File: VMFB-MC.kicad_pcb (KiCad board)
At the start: 2 copper layers, 64.6 x 73.2 mm, 50 parts, among them J1 DISPENSE, J2 EMPTY, J3 DISPENSE, J4 EMPTY, J5 DEPOSIT, J6 DISPENSE, J7 MOTOR, J8 PIR, J9 Conn_01x10_Pin, Q1 Q_Photo_NPN, Q10 Q_Photo_NPN, Q2 Q_Photo_NPN, Q3 Q_Photo_NPN, Q4 Q_Photo_NPN, Q5 Q_Photo_NPN, Q6 Q_Photo_NPN, Q7 TIP120, Q8 TIP120, Q9 BC337, U1 LM393

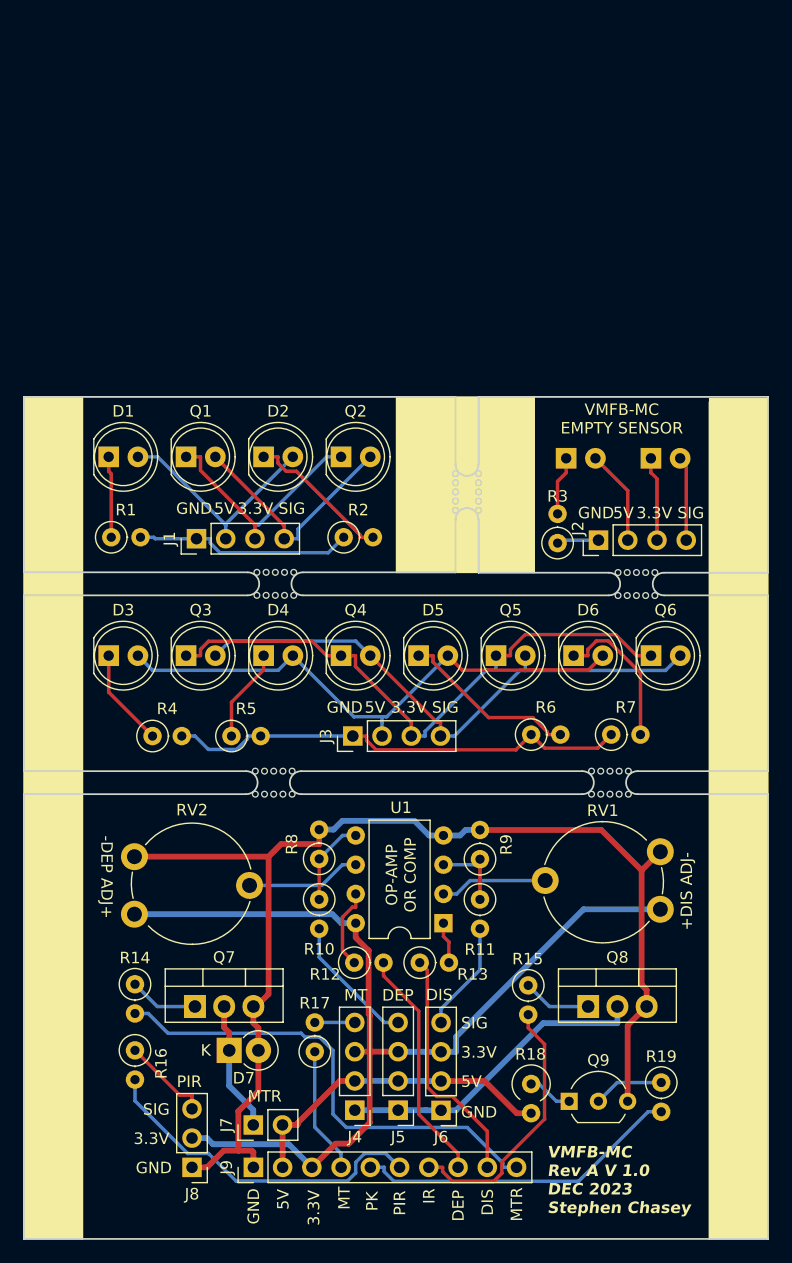
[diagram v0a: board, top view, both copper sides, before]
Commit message: reduced footprint
footprint is now 65x68mm
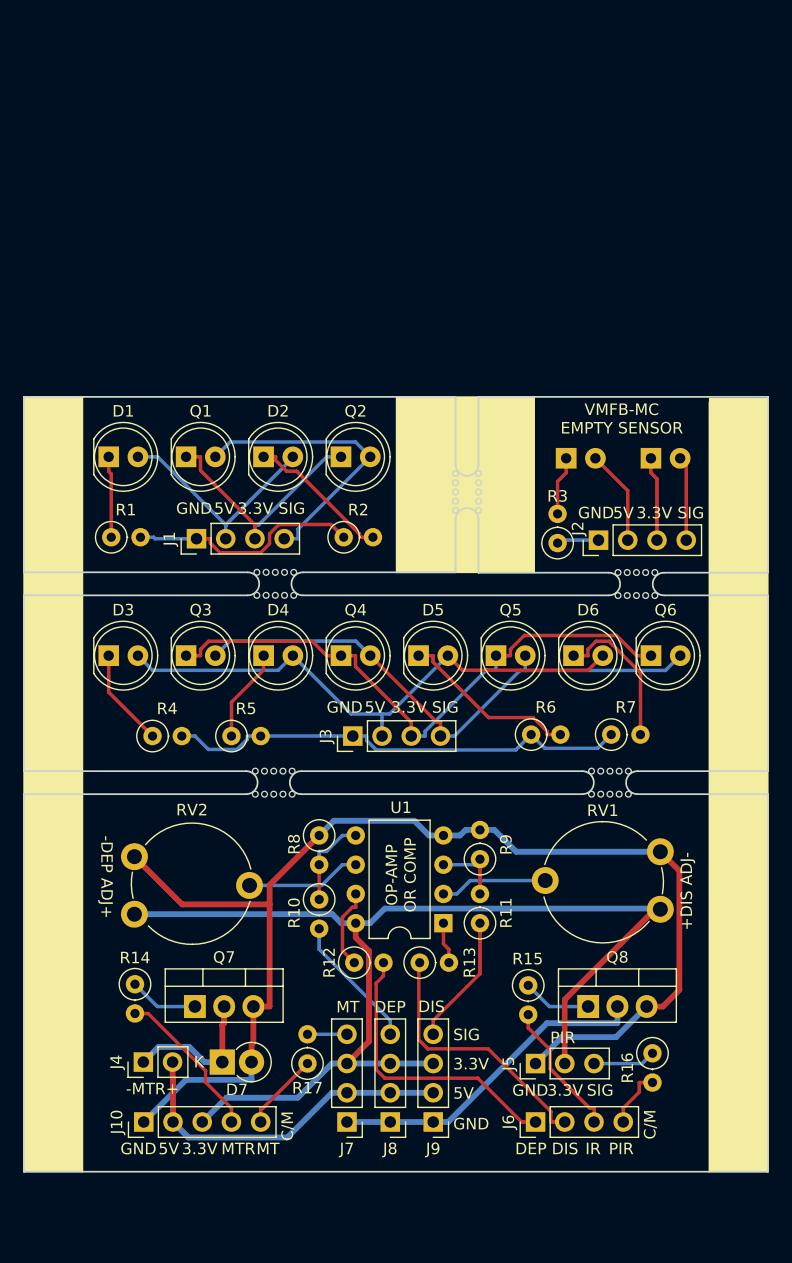
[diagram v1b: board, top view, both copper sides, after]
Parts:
- removed the G*** at (132.6, 103.9)
- removed the J9 at (120.0, 117.0)
- removed the Q9 at (147.4, 111.2)
- removed R18: 47R, Resistor_THT:R_Axial_DIN0309_L9.0mm_D3.2mm_P2.54mm_Vertical
- removed R19: 10K, Resistor_THT:R_Axial_DIN0207_L6.3mm_D2.5mm_P2.54mm_Vertical
- added G***: LOGO, VMFB-MC:VMFB_logo_20mm, B.Cu at (132.7, 97.7)
- added J10: Conn_01x05_Pin, Connector_PinHeader_2.54mm:PinHeader_1x05_P2.54mm_Vertical, F.Cu at (110.5, 113.0)
- added J6: Conn_01x04_Pin, Connector_PinHeader_2.54mm:PinHeader_1x04_P2.54mm_Vertical, F.Cu at (144.5, 113.0)
- moved R16 45.0 mm to (154.7, 107.1)
- moved J5 31.2 mm to (144.5, 108.0), turned to 90 degrees
- moved J4 11.0 mm to (110.5, 107.8)
- moved R11 2.06 mm to (139.7, 95.8), turned to 90 degrees
- moved R8 2.03 mm to (125.7, 88.1), turned to -90 degrees
- moved J7 1.23 mm to (128.1, 113.0)
- moved J8 1.23 mm to (131.9, 113.0)
- moved J9 1.22 mm to (135.6, 113.0)
- moved R17 1.21 mm to (124.7, 108.0)
- moved D7 1.18 mm to (117.3, 107.8)
- renumbered J7 to J4, J8 to J5, J4 to J7, J5 to J8, J6 to J9, Q10 to Q9
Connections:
- R11 pad 1: Net-(U1A-+) -> DISPENSE SIG
- R11 pad 2: DISPENSE SIG -> Net-(U1A-+)
- R8 pad 1: Net-(U1B-+) -> GND
- R8 pad 2: GND -> Net-(U1B-+)
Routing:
- net MOTOR: track 42.1 -> 13.6 mm
- net PBKA: track 28.5 -> 0.00 mm
- net PIR: track 29.8 -> 5.16 mm
- net SENSOR IR: track 23.3 -> 11.9 mm
- net +3.3V: track 87.9 -> 99.3 mm
- net Net-(Q9-B): track 6.14 -> 0.00 mm
- net Net-(J1-Pin_4): track 20.5 -> 25.4 mm
- net DEPOSIT: track 20.5 -> 25.3 mm
- net EMPTY: track 11.0 -> 6.87 mm
- net Net-(Q9-C): track 3.92 -> 0.00 mm
- net GND: track 106.0 -> 108.4 mm
- net Net-(J5-Pin_3): track 7.76 -> 5.45 mm
- net DISPENSE: track 21.0 -> 22.9 mm
- net +5V: track 28.1 -> 30.0 mm
- net DISPENSE SIG: track 9.56 -> 11.3 mm
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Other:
- board size 64.6 x 73.2 mm -> 64.6 x 67.3 mm
- board text added: "-MTR+"
- board text added: "C/M"
- board text removed: "PK"

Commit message: MT bleeder resistor
Added bleeder resistor to the MT sensor.
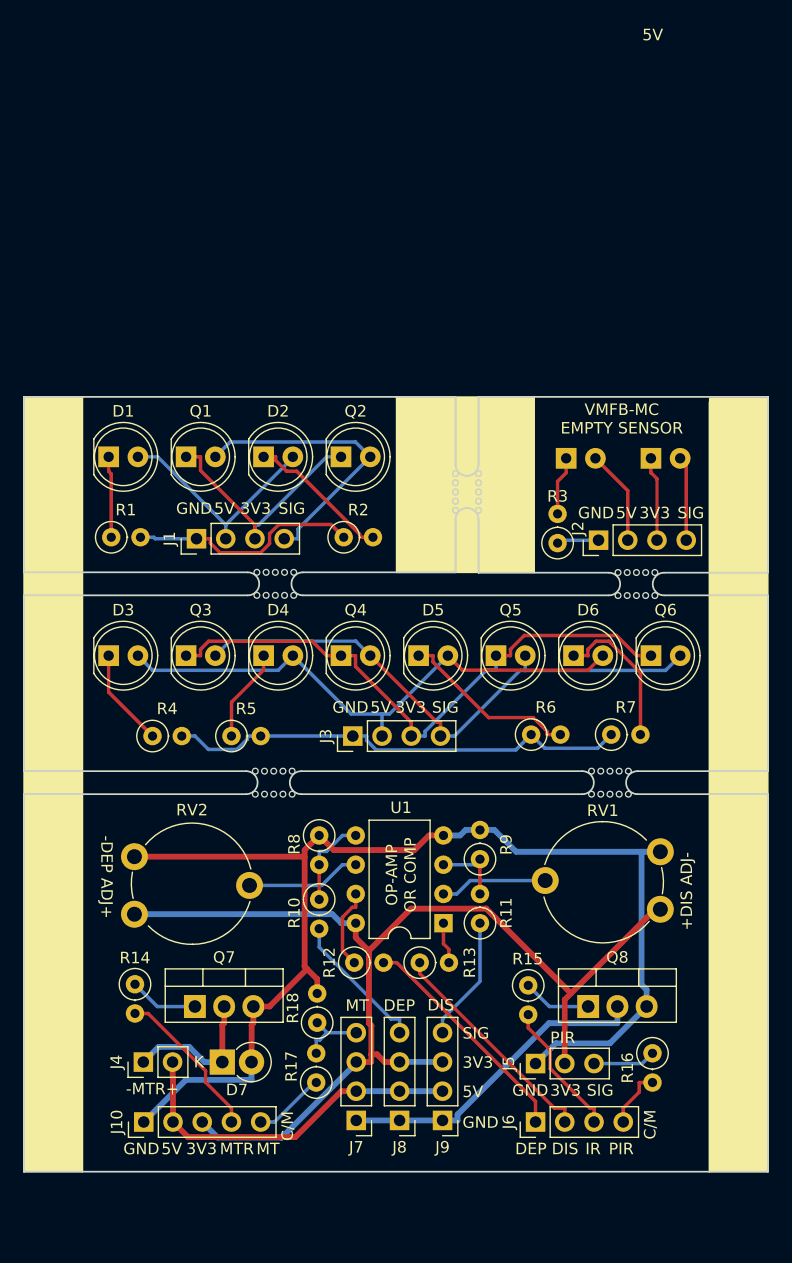
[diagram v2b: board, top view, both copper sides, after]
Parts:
- added R18: 10K, Resistor_THT:R_Axial_DIN0207_L6.3mm_D2.5mm_P2.54mm_Vertical, F.Cu at (125.6, 104.4)
- moved R17 1.82 mm to (125.5, 109.6)
- moved J7 0.82 mm to (129.0, 112.9)
- moved J8 0.82 mm to (132.7, 112.9)
- moved J9 0.82 mm to (136.4, 112.9)
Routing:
- net DEPOSIT: track 25.3 -> 20.0 mm
- net +3.3V: track 99.3 -> 95.9 mm
- net DISPENSE: track 22.9 -> 19.6 mm
- net Net-(J7-Pin_4): track 3.43 -> 6.12 mm
- net GND: track 108.4 -> 109.8 mm
- net +5V: track 30.0 -> 30.8 mm
- net DEPOSIT SIG: track 11.7 -> 12.4 mm
- net EMPTY: track 6.87 -> 6.25 mm
- net IR GND: track 28.5 -> 27.9 mm
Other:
- board text added: "3V3"
- board text removed: "3.3V"

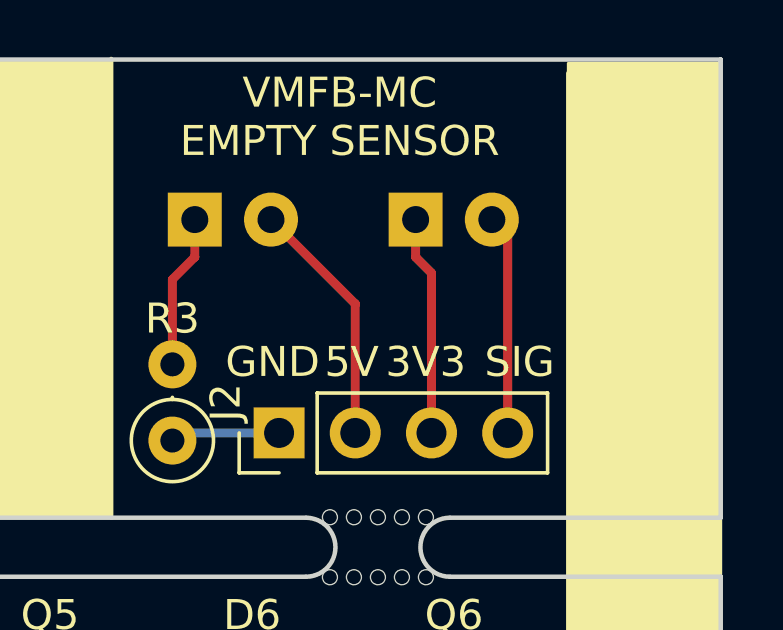
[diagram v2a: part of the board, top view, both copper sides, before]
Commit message: Cleaned up tracks placement on MT sensor
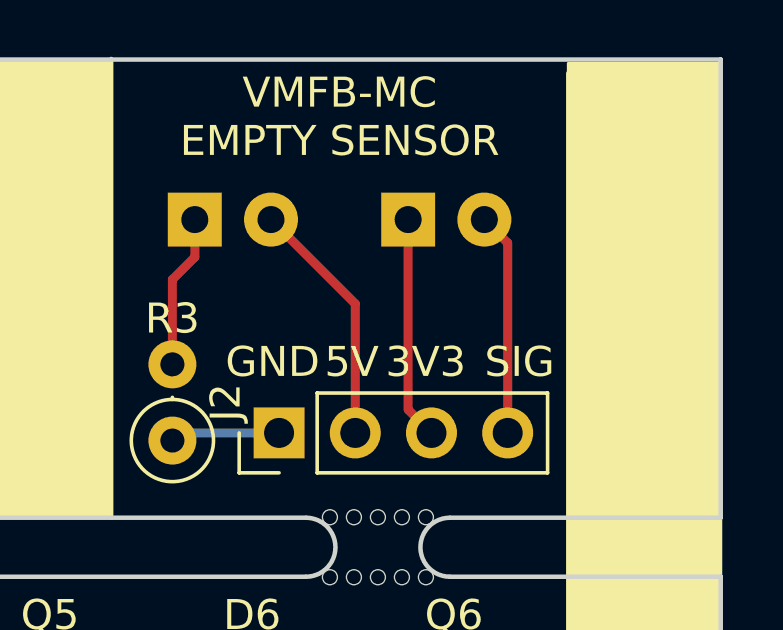
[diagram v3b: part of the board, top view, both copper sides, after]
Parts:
- moved Q9 0.25 mm to (154.3, 55.4)
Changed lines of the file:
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@@
   )
   (footprint "LED_THT:LED_D5.0mm_IRBlack" (layer "B.Cu")
-    (at 154.549 55.372)
+    (at 154.3 55.372)
     (descr "LED, diameter 5.0mm, 2 pins, http://cdn-reichelt.de/documents/datenblatt/A500/LL-504BC2E-009.pdf")
     (tags "LED diameter 5.0mm 2 pins")
@@
   (segment (start 149.997 62.484) (end 146.695 62.484) (width 0.3) (layer "B.Cu") (net 32))
   (segment (start 146.695 62.484) (end 146.441 62.738) (width 0.3) (layer "B.Cu") (net 32))
-  (segment (start 154.549 55.372) (end 154.549 56.6239) (width 0.3) (layer "F.Cu") (net 33))
-  (segment (start 154.549 56.6239) (end 155.077 57.1519) (width 0.3) (layer "F.Cu") (net 33))
-  (segment (start 155.077 57.1519) (end 155.077 62.484) (width 0.3) (layer "F.Cu") (net 33))
-  (segment (start 157.089 55.372) (end 157.617 55.9) (width 0.3) (layer "F.Cu") (net 34))
-  (segment (start 157.617 55.9) (end 157.617 62.484) (width 0.3) (layer "F.Cu") (net 34))
+  (segment (start 154.3 55.372) (end 154.3 61.707) (width 0.3) (layer "F.Cu") (net 33))
+  (segment (start 154.3 61.707) (end 155.077 62.484) (width 0.3) (layer "F.Cu") (net 33))
+  (segment (start 157.617 62.484) (end 157.617 56.149) (width 0.3) (layer "F.Cu") (net 34))
+  (segment (start 157.617 56.149) (end 156.84 55.372) (width 0.3) (layer "F.Cu") (net 34))
   (segment (start 120.65 79.502) (end 119.4981 79.502) (width 0.3) (layer "B.Cu") (net 35))
   (segment (start 116.1063 80.6644) (end 118.6042 80.6644) (width 0.3) (layer "B.Cu") (net 35))

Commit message: Cleaned up BOM naming
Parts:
- J1, J3, J9: value DISPENSE -> Conn_01x04_Pin
- J2, J7: value EMPTY -> Conn_01x04_Pin
- J4: value MOTOR -> Conn_01x02_Pin
- J5: value PIR -> Conn_01x03_Pin
- J8: value DEPOSIT -> Conn_01x04_Pin
- Q1, Q2, Q3, Q4, Q5, Q6, Q9: value Q_Photo_NPN -> SFH313FA-2/3
- R14, R15: value 1K -> 10K
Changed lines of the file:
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@@
         (effects (font (size 1 1) (thickness 0.15)))
     )
-    (fp_text value "EMPTY" (at 0 9.95 90) (layer "F.Fab")
+    (fp_text value "Conn_01x04_Pin" (at 0 9.95 90) (layer "F.Fab")
         (effects (font (size 1 1) (thickness 0.15)))
     )
@@
         (effects (font (size 1 1) (thickness 0.15)))
     )
-    (fp_text value "PIR" (at 0 7.41 90) (layer "F.Fab")
+    (fp_text value "Conn_01x03_Pin" (at 0 7.41 90) (layer "F.Fab")
         (effects (font (size 1 1) (thickness 0.15)))
     )
@@
         (effects (font (size 1 1) (thickness 0.15)))
     )
-    (fp_text value "Q_Photo_NPN" (at 1.27 3.96) (layer "F.Fab")
+    (fp_text value "SFH313FA-2/3" (at 1.27 3.96) (layer "F.Fab")
         (effects (font (size 1 1) (thickness 0.15)))
     )
@@
         (effects (font (size 1 1) (thickness 0.15)))
     )
-    (fp_text value "Q_Photo_NPN" (at 1.27 3.96) (layer "F.Fab")
+    (fp_text value "SFH313FA-2/3" (at 1.27 3.96) (layer "F.Fab")
         (effects (font (size 1 1) (thickness 0.15)))
     )
@@
         (effects (font (size 1 1) (thickness 0.15)))
     )
-    (fp_text value "MOTOR" (at 0 4.87 90) (layer "F.Fab")
+    (fp_text value "Conn_01x02_Pin" (at 0 4.87 90) (layer "F.Fab")
         (effects (font (size 1 1) (thickness 0.15)))
     )
@@
         (effects (font (size 1 1) (thickness 0.15)))
     )
-    (fp_text value "EMPTY" (at 0 9.95) (layer "F.Fab")
+    (fp_text value "Conn_01x04_Pin" (at 0 9.95) (layer "F.Fab")
         (effects (font (size 1 1) (thickness 0.15)))
     )
@@
         (effects (font (size 1 1) (thickness 0.15)))
     )
-    (fp_text value "DISPENSE" (at 0 9.95 90) (layer "F.Fab")
+    (fp_text value "Conn_01x04_Pin" (at 0 9.95 90) (layer "F.Fab")
         (effects (font (size 1 1) (thickness 0.15)))
     )
@@
         (effects (font (size 1 1) (thickness 0.15)))
     )
-    (fp_text value "Q_Photo_NPN" (at 1.27 3.96) (layer "F.Fab")
+    (fp_text value "SFH313FA-2/3" (at 1.27 3.96) (layer "F.Fab")
         (effects (font (size 1 1) (thickness 0.15)))
     )
@@
         (effects (font (size 1 1) (thickness 0.15)))
     )
-    (fp_text value "DISPENSE" (at 0 9.95 90) (layer "F.Fab")
+    (fp_text value "Conn_01x04_Pin" (at 0 9.95 90) (layer "F.Fab")
         (effects (font (size 1 1) (thickness 0.15)))
     )
@@
         (effects (font (size 1 1) (thickness 0.15)))
     )
-    (fp_text value "Q_Photo_NPN" (at 1.27 3.96) (layer "F.Fab")
+    (fp_text value "SFH313FA-2/3" (at 1.27 3.96) (layer "F.Fab")
         (effects (font (size 1 1) (thickness 0.15)))
     )
@@
         (effects (font (size 1 1) (thickness 0.15)))
     )
-    (fp_text value "DISPENSE" (at 0 9.95) (layer "F.Fab")
+    (fp_text value "Conn_01x04_Pin" (at 0 9.95) (layer "F.Fab")
         (effects (font (size 1 1) (thickness 0.15)))
     )
@@
         (effects (font (size 1 1) (thickness 0.15)))
     )
-    (fp_text value "Q_Photo_NPN" (at 1.27 3.96) (layer "F.Fab")
+    (fp_text value "SFH313FA-2/3" (at 1.27 3.96) (layer "F.Fab")
         (effects (font (size 1 1) (thickness 0.15)))
     )
@@
         (effects (font (size 1 1) (thickness 0.15)))
     )
-    (fp_text value "Q_Photo_NPN" (at 1.27 3.96) (layer "F.Fab")
+    (fp_text value "SFH313FA-2/3" (at 1.27 3.96) (layer "F.Fab")
         (effects (font (size 1 1) (thickness 0.15)))
     )
@@
         (effects (font (size 1 1) (thickness 0.15)))
     )
-    (fp_text value "DEPOSIT" (at 0 9.95) (layer "F.Fab")
+    (fp_text value "Conn_01x04_Pin" (at 0 9.95) (layer "F.Fab")
         (effects (font (size 1 1) (thickness 0.15)))
     )
@@
         (effects (font (size 1 1) (thickness 0.15)))
     )
-    (fp_text value "1K" (at 1.27 2.37 90) (layer "F.Fab")
+    (fp_text value "10K" (at 1.27 2.37 90) (layer "F.Fab")
         (effects (font (size 1 1) (thickness 0.15)))
     )
@@
         (effects (font (size 1 1) (thickness 0.15)))
     )
-    (fp_text value "1K" (at 1.27 2.37 90) (layer "F.Fab")
+    (fp_text value "10K" (at 1.27 2.37 90) (layer "F.Fab")
         (effects (font (size 1 1) (thickness 0.15)))
     )
@@
         (effects (font (size 1 1) (thickness 0.15)) (justify mirror))
     )
-    (fp_text value "Q_Photo_NPN" (at 1.27 -3.96) (layer "B.Fab")
+    (fp_text value "SFH313FA-2/3" (at 1.27 -3.96) (layer "B.Fab")
         (effects (font (size 1 1) (thickness 0.15)) (justify mirror))
     )
